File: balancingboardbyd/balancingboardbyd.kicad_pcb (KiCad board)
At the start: 2 copper layers, 50 x 50 mm, 74 parts, among them CN1 XT30PW-M, CN2 WJ15EDGRC-3.81-4P, CN3 WJ15EDGRC-3.81-4P, Q1 KMBTA94, Q10 SI2302A-TP, Q11 IRFH5302TRPBF, Q2 SI2302A-TP, Q3 SI2302A-TP, Q4 SI2302A-TP, Q5 SI2302A-TP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

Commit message: base balancing byd
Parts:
- CN1, U3: moved to B.Cu
- moved C3 119.9 mm to (205.3, 46.3)
- moved R24 119.5 mm to (205.7, 75.3)
- moved C4 118.6 mm to (203.9, 48.5)
- moved C5 118.5 mm to (204.3, 53.3), turned to 90 degrees
- moved Rccv2 107.3 mm to (209.3, 46.3), turned to 180 degrees
- moved CN1 100.6 mm to (208.3, 88.9), turned to 180 degrees
- moved C19 100.3 mm to (196.9, 71.3)
- moved U3 97.6 mm to (190.8, 91.5), turned to 180 degrees
- moved Q7 97.1 mm to (198.5, 85.6)
- moved D1 96.7 mm to (191.1, 81.2), turned to 90 degrees
- moved Rccv1 96.5 mm to (202.7, 57.8), turned to -90 degrees
- moved Q11 92.7 mm to (198.5, 78.2), turned to 180 degrees
- moved D2 91.2 mm to (185.3, 83.7), turned to 90 degrees
- moved RDO1 88.3 mm to (192.6, 72.2), turned to -90 degrees
- moved RCO1 85.7 mm to (191.1, 85.8), turned to 90 degrees
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
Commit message: next step
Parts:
- added BT1: BH-18650-B1BA007, easyeda2kicad:BAT-SMD_BH-18650-B1BA007, F.Cu at (286.9, 150.1)
- added BT2: BH-18650-B1BA007, easyeda2kicad:BAT-SMD_BH-18650-B1BA007, B.Cu at (286.9, 150.2)
- added BT3: BH-18650-B1BA007, easyeda2kicad:BAT-SMD_BH-18650-B1BA007, B.Cu at (286.6, 55.0)
- added U4: BH-21700-B1BJ001, easyeda2kicad:BAT-SMD_L82.5.5-W25-BH-21700-B1BJ001, F.Cu at (274.8, 150.1)
- added U5: BH-21700-B1BJ001, easyeda2kicad:BAT-SMD_L82.5.5-W25-BH-21700-B1BJ001, F.Cu at (300.4, 150.1)
- added U6: BH-21700-B1BJ001, easyeda2kicad:BAT-SMD_L82.5.5-W25-BH-21700-B1BJ001, B.Cu at (274.8, 150.0)
- added U7: BH-21700-B1BJ001, easyeda2kicad:BAT-SMD_L82.5.5-W25-BH-21700-B1BJ001, B.Cu at (300.4, 150.1)
- added U8: BH-21700-B1BJ001, easyeda2kicad:BAT-SMD_L82.5.5-W25-BH-21700-B1BJ001, B.Cu at (300.4, 55.4)
- added U9: BH-21700-B1BJ001, easyeda2kicad:BAT-SMD_L82.5.5-W25-BH-21700-B1BJ001, B.Cu at (274.8, 55.5)
- moved C13 100.8 mm to (93.3, 28.2)
- moved C15 100.8 mm to (93.3, 30.2)
- moved C17 100.8 mm to (93.3, 32.1)
- moved C3 100.8 mm to (109.8, 14.1)
- moved C5 100.8 mm to (108.8, 21.1)
- moved CN1 100.8 mm to (112.8, 56.7)
- moved D2 100.8 mm to (89.8, 51.5)
- moved Q11 100.8 mm to (103.0, 46.0)
- moved Q7 100.8 mm to (103.0, 53.4)
- moved R11 100.8 mm to (127.4, 21.2)
- moved R14 100.8 mm to (127.4, 28.7)
- moved R16 100.8 mm to (127.4, 31.2)
- moved R18 100.8 mm to (127.4, 18.7)
- moved R25 100.8 mm to (127.4, 23.7)
- moved R27 100.8 mm to (127.4, 26.2)
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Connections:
- CN1 pad 2: BAT+ -> B8
- U3 pad 1: BAT+ -> B8
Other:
- board size 50 x 50 mm -> 55.6 x 191 mm

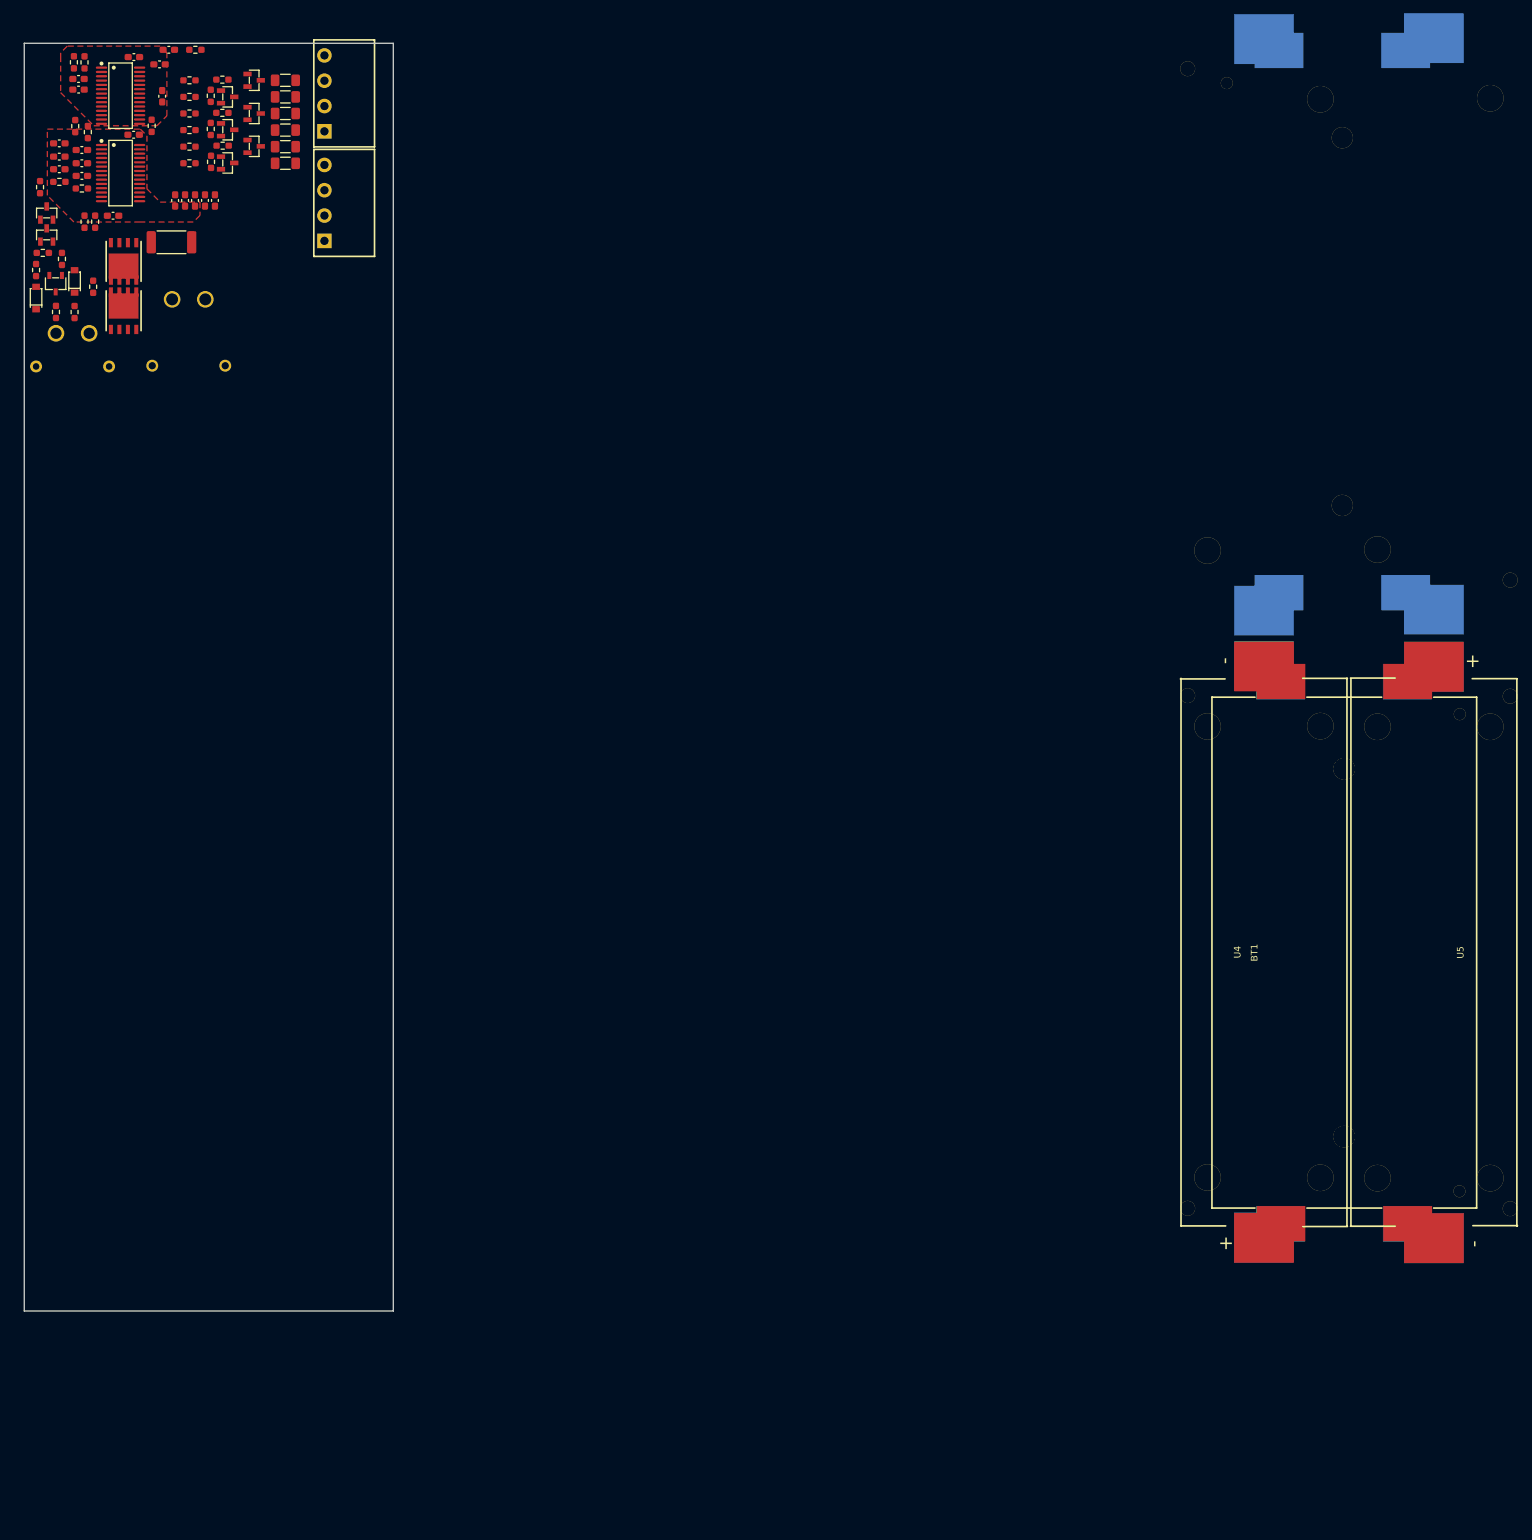
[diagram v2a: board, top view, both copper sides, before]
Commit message: balancing board route
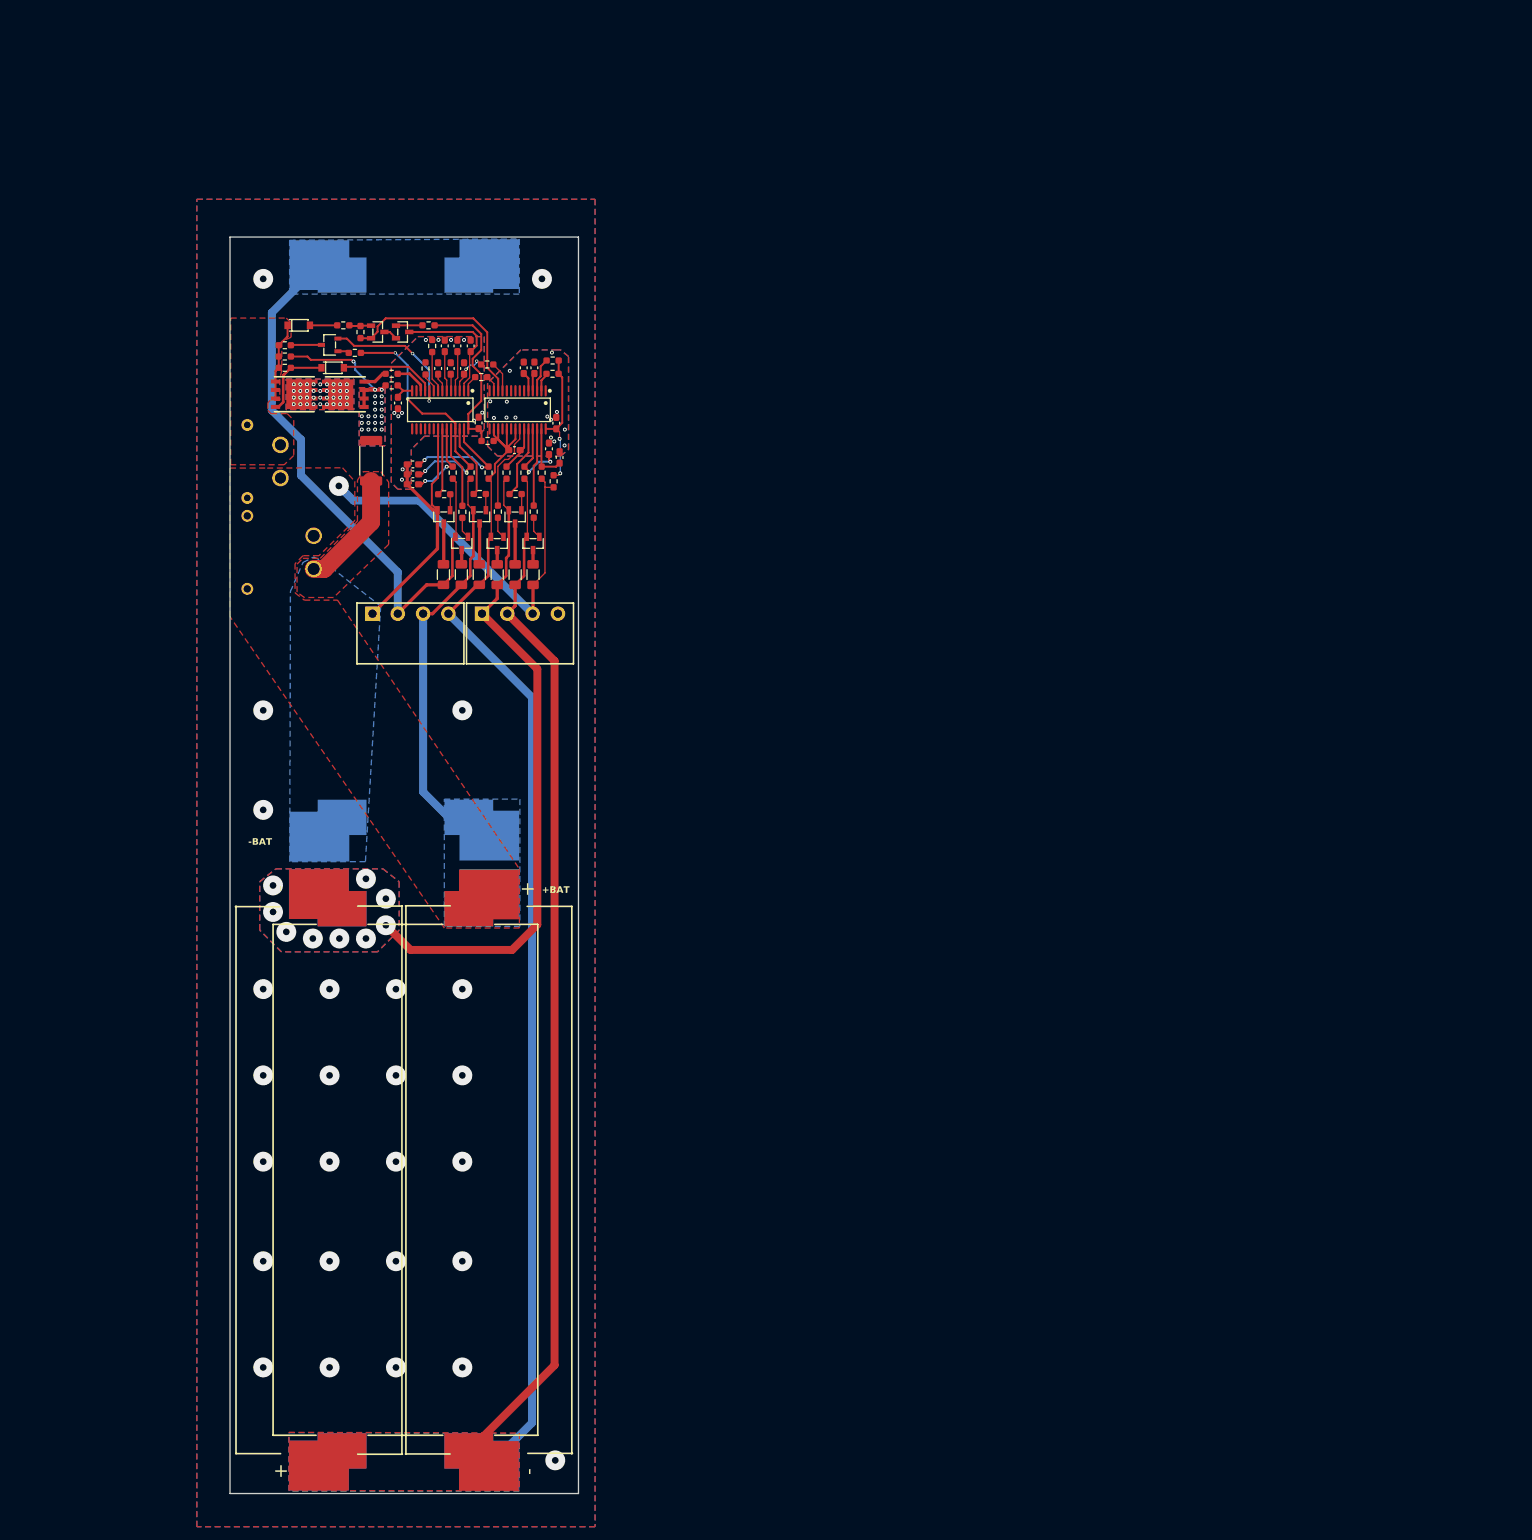
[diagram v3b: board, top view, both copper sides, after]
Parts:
- removed C11, C12: 0.1uF, Capacitor_SMD:C_0603_1608Metric_Pad1.08x0.95mm_HandSolder
- moved U5 171.4 mm to (132.4, 184.4), turned to 90 degrees
- moved U6 146.5 mm to (132.4, 184.3)
- moved U7 146.4 mm to (158.1, 184.3)
- moved U9 146.3 mm to (132.5, 89.6)
- moved U8 146.3 mm to (158.1, 89.4)
- moved BT1 145.5 mm to (145.4, 184.3), turned to -90 degrees
- moved BT2 145.5 mm to (145.4, 184.3)
- moved BT3 145.2 mm to (145.4, 88.9)
- moved U4 121.7 mm to (158.0, 184.4), turned to -90 degrees
- moved C3 85.1 mm to (168.7, 75.5), turned to -90 degrees
- moved R2 85.0 mm to (167.6, 60.9), turned to 180 degrees
- moved R1 84.7 mm to (167.6, 62.9), turned to 180 degrees
- moved Rccv2 84.5 mm to (167.8, 79.1), turned to 90 degrees
- moved C6 84.2 mm to (168.2, 70.4), turned to -90 degrees
- moved CN2 83.7 mm to (162.7, 99.1), turned to 0 degrees
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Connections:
- Q6 pad 2: Net-(Q1-E) -> Net-(Q1-C)
- RP1 pad 1: Net-(Q1-C) -> Net-(Q1-E)
- U1 pad 12: Net-(Q1-C) -> Net-(Q1-E)
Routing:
- net B5: track 0.00 -> 180.1 mm, vias 0 -> 14
- net B7: track 0.00 -> 156.2 mm
- net B6: track 0.00 -> 98.7 mm, vias 0 -> 9
- net B3: track 0.00 -> 89.0 mm
- net B4: track 0.00 -> 60.1 mm
- net B8: track 0.00 -> 59.8 mm, vias 0 -> 1
- net BSET: track 0.00 -> 59.6 mm, vias 0 -> 37
- net /VC4: track 0.00 -> 39.0 mm, vias 0 -> 4
- net Net-(Q1-E): track 0.00 -> 31.2 mm
- net VCC1: track 0.00 -> 27.4 mm
- net Net-(Q8-S): track 0.00 -> 21.9 mm, vias 0 -> 2
- net Net-(Q11-S-Pad1): track 0.00 -> 21.4 mm, vias 0 -> 21
- net VCC2: track 0.00 -> 20.6 mm, vias 0 -> 2
- net DOIN: track 0.00 -> 19.4 mm
- net /VC5: track 0.00 -> 18.9 mm, vias 0 -> 2
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- added copper zone on B.Cu, net B3
- added copper zone on B.Cu, net B4
- added copper zone on B.Cu, net B5
- added copper zone on B.Cu, net B6
- added copper zone on F.Cu, net B6
- added copper zone on F.Cu, net B7
- added copper zone on F.Cu, net B8
- added copper zone on B.Cu, net BSET
- added copper zone on F.Cu, net BSET
- added copper zone on B.Cu, net Net-(Q11-S-Pad1)
- added copper zone on F.Cu, net Net-(Q11-S-Pad1)
- added copper zone on B.Cu, net O-
- added copper zone on F.Cu, net O-
- added copper zone on F.Cu, net PACK-
- removed copper zone on F.Cu, net (none)
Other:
- board size 55.6 x 191 mm -> 52.5 x 189.3 mm
- board text added: "+BAT"
- board text added: "-BAT"

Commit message: add logo
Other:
- board text added: "Janek"
- board text added: "github.com/janekc"

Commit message: kurz vor bestellung
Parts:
- removed CN2, CN3: WJ15EDGRC-3.81-4P, easyeda2kicad:CONN-TH_WJ15EDGRC-3.81-4P
- added CN4: WJ15EDGVC-3.81-4P, easyeda2kicad:CONN-TH_4P-P3.81_WJ2EDGVC-3.81-4P, F.Cu at (162.7, 99.1)
- added CN5: WJ15EDGVC-3.81-4P, easyeda2kicad:CONN-TH_4P-P3.81_WJ2EDGVC-3.81-4P, F.Cu at (146.2, 99.1)
